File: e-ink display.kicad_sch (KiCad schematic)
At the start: 20 parts, among them Q1 AO3400A

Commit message: WIP
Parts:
- D1, D2, D3: value MBR0530 -> B5819W; LCSC C475718 -> C7420330
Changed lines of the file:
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@@
     (pin "2")
     (instances
-      (project "USB E-Ink thing"
+      (project "USB E-Paper thing"
         (path "/03659e82-b7b8-4d3e-8633-26f17364684b"
           (reference "C5") (unit 1)
@@
     (pin "2")
     (instances
-      (project "USB E-Ink thing"
+      (project "USB E-Paper thing"
         (path "/03659e82-b7b8-4d3e-8633-26f17364684b"
           (reference "C10") (unit 1)
@@
     (pin "1")
     (instances
-      (project "USB E-Ink thing"
+      (project "USB E-Paper thing"
         (path "/03659e82-b7b8-4d3e-8633-26f17364684b"
           (reference "#PWR04") (unit 1)
@@
       (effects (font (size 1.27 1.27)) (justify right))
     )
-    (property "Value" "MBR0530" (at 159.512 82.8096 90)
+    (property "Value" "B5819W" (at 159.512 82.8096 90)
       (effects (font (size 1.27 1.27)) (justify right))
     )
@@
       (effects (font (size 1.27 1.27)) hide)
     )
-    (property "LCSC" "C475718" (at 157.48 81.28 0)
-      (effects (font (size 1.27 1.27)) hide)
-    )
-    (pin "1")
-    (pin "2")
-    (instances
-      (project "USB E-Ink thing"
+    (property "LCSC" "C7420330" (at 157.48 81.28 0)
+      (effects (font (size 1.27 1.27)) hide)
+    )
+    (pin "1")
+    (pin "2")
+    (instances
+      (project "USB E-Paper thing"
         (path "/03659e82-b7b8-4d3e-8633-26f17364684b"
           (reference "D2") (unit 1)
@@
     (pin "3")
     (instances
-      (project "USB E-Ink thing"
+      (project "USB E-Paper thing"
         (path "/03659e82-b7b8-4d3e-8633-26f17364684b"
           (reference "Q1") (unit 1)
@@
     (pin "1")
     (instances
-      (project "USB E-Ink thing"
+      (project "USB E-Paper thing"
         (path "/03659e82-b7b8-4d3e-8633-26f17364684b"
           (reference "#PWR028") (unit 1)
@@
     (pin "2")
     (instances
-      (project "USB E-Ink thing"
+      (project "USB E-Paper thing"
         (path "/03659e82-b7b8-4d3e-8633-26f17364684b"
           (reference "C3") (unit 1)
@@
       (effects (font (size 1.27 1.27)) (justify left))
     )
-    (property "Value" "MBR0530" (at 177.292 82.1746 90)
+    (property "Value" "B5819W" (at 177.292 82.1746 90)
       (effects (font (size 1.27 1.27)) (justify left))
     )
@@
       (effects (font (size 1.27 1.27)) hide)
     )
-    (property "LCSC" "C475718" (at 175.26 81.28 0)
-      (effects (font (size 1.27 1.27)) hide)
-    )
-    (pin "1")
-    (pin "2")
-    (instances
-      (project "USB E-Ink thing"
+    (property "LCSC" "C7420330" (at 175.26 81.28 0)
+      (effects (font (size 1.27 1.27)) hide)
+    )
+    (pin "1")
+    (pin "2")
+    (instances
+      (project "USB E-Paper thing"
         (path "/03659e82-b7b8-4d3e-8633-26f17364684b"
           (reference "D3") (unit 1)
@@
     (pin "1")
     (instances
-      (project "USB E-Ink thing"
+      (project "USB E-Paper thing"
         (path "/03659e82-b7b8-4d3e-8633-26f17364684b/4dbcbaef-7c6d-4c27-8e2b-a8b0ba0cdd01"
           (reference "#FLG06") (unit 1)
@@
     (pin "2")
     (instances
-      (project "USB E-Ink thing"
+      (project "USB E-Paper thing"
         (path "/03659e82-b7b8-4d3e-8633-26f17364684b"
           (reference "C11") (unit 1)
@@
     (pin "1")
     (instances
-      (project "USB E-Ink thing"
+      (project "USB E-Paper thing"
         (path "/03659e82-b7b8-4d3e-8633-26f17364684b"
           (reference "#PWR07") (unit 1)
@@
     (pin "2")
     (instances
-      (project "USB E-Ink thing"
+      (project "USB E-Paper thing"
         (path "/03659e82-b7b8-4d3e-8633-26f17364684b"
           (reference "C6") (unit 1)
@@
     (pin "2")
     (instances
-      (project "USB E-Ink thing"
+      (project "USB E-Paper thing"
         (path "/03659e82-b7b8-4d3e-8633-26f17364684b"
           (reference "C8") (unit 1)
@@
     (pin "1")
     (instances
-      (project "USB E-Ink thing"
+      (project "USB E-Paper thing"
         (path "/03659e82-b7b8-4d3e-8633-26f17364684b"
           (reference "#PWR05") (unit 1)
@@
     (pin "1")
     (instances
-      (project "USB E-Ink thing"
+      (project "USB E-Paper thing"
         (path "/03659e82-b7b8-4d3e-8633-26f17364684b"
           (reference "#PWR012") (unit 1)
@@
     (pin "2")
     (instances
-      (project "USB E-Ink thing"
+      (project "USB E-Paper thing"
         (path "/03659e82-b7b8-4d3e-8633-26f17364684b"
           (reference "R1") (unit 1)
@@
     (pin "2")
     (instances
-      (project "USB E-Ink thing"
+      (project "USB E-Paper thing"
         (path "/03659e82-b7b8-4d3e-8633-26f17364684b"
           (reference "C2") (unit 1)
@@
     (pin "1")
     (instances
-      (project "USB E-Ink thing"
+      (project "USB E-Paper thing"
         (path "/03659e82-b7b8-4d3e-8633-26f17364684b"
           (reference "#PWR08") (unit 1)
@@
     (pin "2")
     (instances
-      (project "USB E-Ink thing"
+      (project "USB E-Paper thing"
         (path "/03659e82-b7b8-4d3e-8633-26f17364684b"
           (reference "C4") (unit 1)
@@
     (pin "1")
     (instances
-      (project "USB E-Ink thing"
+      (project "USB E-Paper thing"
         (path "/03659e82-b7b8-4d3e-8633-26f17364684b"
           (reference "#PWR010") (unit 1)
@@
       (effects (font (size 1.27 1.27)))
     )
-    (property "Value" "MBR0530" (at 144.4625 89.7199 0)
+    (property "Value" "B5819W" (at 144.4625 89.7199 0)
       (effects (font (size 1.27 1.27)))
     )
@@
       (effects (font (size 1.27 1.27)) hide)
     )
-    (property "LCSC" "C475718" (at 144.78 92.71 0)
-      (effects (font (size 1.27 1.27)) hide)
-    )
-    (pin "1")
-    (pin "2")
-    (instances
-      (project "USB E-Ink thing"
+    (property "LCSC" "C7420330" (at 144.78 92.71 0)
+      (effects (font (size 1.27 1.27)) hide)
+    )
+    (pin "1")
+    (pin "2")
+    (instances
+      (project "USB E-Paper thing"
         (path "/03659e82-b7b8-4d3e-8633-26f17364684b"
           (reference "D1") (unit 1)
@@
     (pin "1")
     (instances
-      (project "USB E-Ink thing"
+      (project "USB E-Paper thing"
         (path "/03659e82-b7b8-4d3e-8633-26f17364684b"
           (reference "#PWR02") (unit 1)
@@
     (pin "1")
     (instances
-      (project "USB E-Ink thing"
+      (project "USB E-Paper thing"
         (path "/03659e82-b7b8-4d3e-8633-26f17364684b"
           (reference "#PWR013") (unit 1)
@@
     (pin "2")
     (instances
-      (project "USB E-Ink thing"
+      (project "USB E-Paper thing"
         (path "/03659e82-b7b8-4d3e-8633-26f17364684b"
           (reference "L1") (unit 1)
@@
     (pin "1")
     (instances
-      (project "USB E-Ink thing"
+      (project "USB E-Paper thing"
         (path "/03659e82-b7b8-4d3e-8633-26f17364684b"
           (reference "#PWR01") (unit 1)
@@
     (pin "1")
     (instances
-      (project "USB E-Ink thing"
+      (project "USB E-Paper thing"
         (path "/03659e82-b7b8-4d3e-8633-26f17364684b"
           (reference "#PWR011") (unit 1)
@@
     (pin "2")
     (instances
-      (project "USB E-Ink thing"
+      (project "USB E-Paper thing"
         (path "/03659e82-b7b8-4d3e-8633-26f17364684b"
           (reference "C1") (unit 1)
@@
     (pin "1")
     (instances
-      (project "USB E-Ink thing"
+      (project "USB E-Paper thing"
         (path "/03659e82-b7b8-4d3e-8633-26f17364684b"
           (reference "#PWR03") (unit 1)
@@
     (pin "2")
     (instances
-      (project "USB E-Ink thing"
+      (project "USB E-Paper thing"
         (path "/03659e82-b7b8-4d3e-8633-26f17364684b"
           (reference "C9") (unit 1)
@@
     (pin "5")
     (instances
-      (project "USB E-Ink thing"
+      (project "USB E-Paper thing"
         (path "/03659e82-b7b8-4d3e-8633-26f17364684b/4dbcbaef-7c6d-4c27-8e2b-a8b0ba0cdd01"
           (reference "DS1") (unit 1)
@@
     (pin "2")
     (instances
-      (project "USB E-Ink thing"
+      (project "USB E-Paper thing"
         (path "/03659e82-b7b8-4d3e-8633-26f17364684b"
           (reference "C5") (unit 1)
@@
     (pin "1")
     (instances
-      (project "USB E-Ink thing"
+      (project "USB E-Paper thing"
         (path "/03659e82-b7b8-4d3e-8633-26f17364684b"
           (reference "#PWR09") (unit 1)
@@
     (pin "1")
     (instances
-      (project "USB E-Ink thing"
+      (project "USB E-Paper thing"
         (path "/03659e82-b7b8-4d3e-8633-26f17364684b"
           (reference "#PWR02") (unit 1)
@@
     (pin "2")
     (instances
-      (project "USB E-Ink thing"
+      (project "USB E-Paper thing"
         (path "/03659e82-b7b8-4d3e-8633-26f17364684b"
           (reference "C7") (unit 1)
@@
     (pin "2")
     (instances
-      (project "USB E-Ink thing"
+      (project "USB E-Paper thing"
         (path "/03659e82-b7b8-4d3e-8633-26f17364684b"
           (reference "C1") (unit 1)
@@
     (pin "1")
     (instances
-      (project "USB E-Ink thing"
+      (project "USB E-Paper thing"
         (path "/03659e82-b7b8-4d3e-8633-26f17364684b"
           (reference "#PWR06") (unit 1)

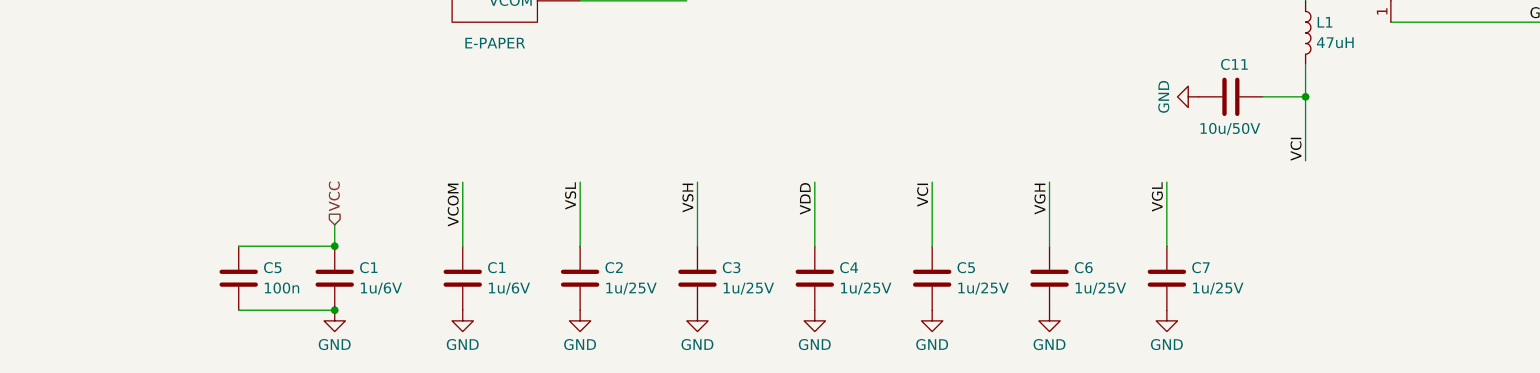
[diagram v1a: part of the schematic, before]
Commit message: Fix all DRC violations, fix 12 MHz crystal connections
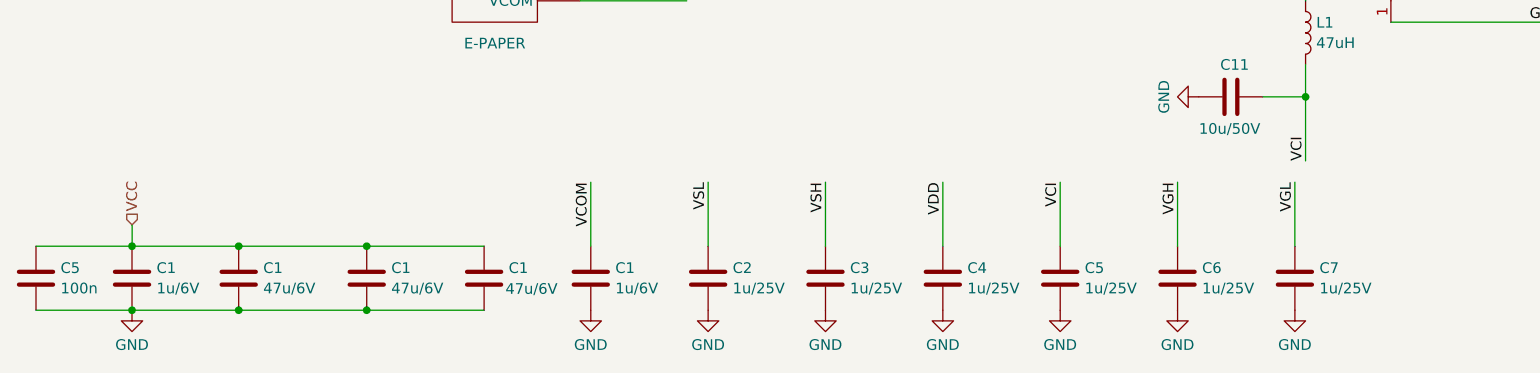
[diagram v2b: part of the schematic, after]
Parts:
- added C1 (x3): 47u/6V, Capacitor_SMD:C_0805_2012Metric, symbol Device:C
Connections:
- net GND: now also C1.2, C1.2, C1.2
- net VCC: now also C1.1, C1.1, C1.1
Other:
- moved on the sheet: C1, C2, C3, C4, C5, C6, C7
